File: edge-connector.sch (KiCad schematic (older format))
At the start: 3 parts, among them J5 SFF-TA-1002-4C+

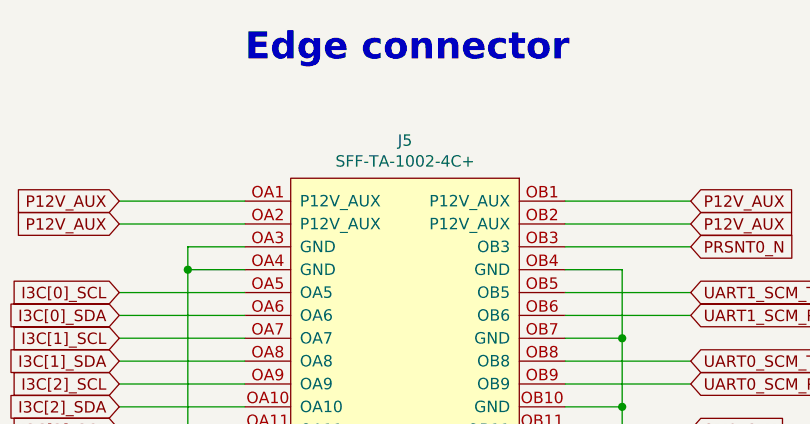
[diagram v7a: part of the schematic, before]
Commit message: Update edge connector
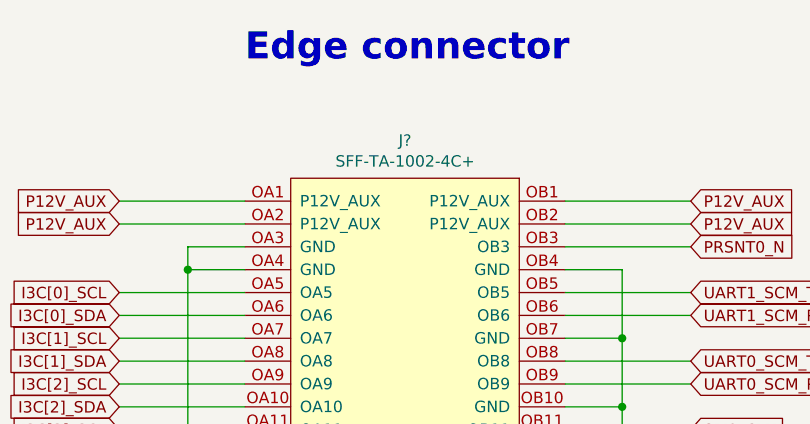
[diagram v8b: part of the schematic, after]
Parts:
- removed J5: SFF-TA-1002-4C+, artix-dc-scm-footprints:SFF-TA-1002-4C+, symbol artix-dc-scm:SFF-TA-1002-4C+
- added J?: SFF-TA-1002-4C+, artix-dc-scm-footprints:SFF-TA-1002-4C+, symbol artix-dc-scm:SFF-TA-1002-4C+
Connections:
- net 3V0_BAT: now also J?.B41
- net CHASI#: now also J?.A54
- net DBP_PRDY_N: now also J?.A50
- net DBP_PREQ_N: now also J?.A49
- net ESPI_ALERT_N: now also J?.B3
- net ESPI_CLK: now also J?.B1
- net ESPI_CS0_N: now also J?.B2
- net ESPI_CS1_N: now also J?.B9
- net ESPI_IO0: now also J?.B5
- net ESPI_IO1: now also J?.B6
- net ESPI_IO2: now also J?.B7
- net ESPI_IO3: now also J?.B8
- net ESPI_RESET_N: now also J?.B4
- net GND: now also J?.A11 (GND), J?.A14 (GND), J?.A17 (GND), J?.A20 (GND), J?.A33 (GND), J?.A42 (GND), J?.A58 (GND), J?.A61 (GND), J?.A64 (GND), J?.A67 (GND), J?.A70 (GND), J?.B10 (GND), J?.B17 (GND), J?.B26 (GND), J?.B33 (GND), J?.B38 (GND), J?.B49 (GND), J?.B52 (GND), J?.B55 (GND), J?.B58 (GND), J?.B61 (GND), J?.B64 (GND), J?.B67 (GND), J?.B70 (GND), J?.OA13 (GND), J?.OA3 (GND), J?.OA4 (GND), J?.OB10 (GND), J?.OB4 (GND), J?.OB7 (GND)
- net HPM_FW_RECOVERY: now also J?.A43
- net HPM_STBY_EN: now also J?.A45
- net HPM_STBY_RDY: now also J?.A44
- net HPM_STBY_RST_N: now also J?.A46
- net I2C[0]_SCL: now also J?.A1
- net I2C[0]_SDA: now also J?.A2
- net I2C[10]_SCL: now also J?.A31
- net I2C[10]_SDA: now also J?.A32
- net I2C[11]_SCL: now also J?.A38
- net I2C[11]_SDA: now also J?.A39
- net I2C[12]_SCL: now also J?.A40
- net I2C[12]_SDA: now also J?.A41
- net I2C[1]_SCL: now also J?.A3
- net I2C[1]_SDA: now also J?.A4
- net I2C[2]_SCL: now also J?.A5
- net I2C[2]_SDA: now also J?.A6
- net I2C[3]_SCL: now also J?.A7
- net I2C[3]_SDA: now also J?.A8
- net I2C[4]_SCL: now also J?.A9
- net I2C[4]_SDA: now also J?.A10
- net I2C[5]_SCL: now also J?.A21
- net I2C[5]_SDA: now also J?.A22
- net I2C[6]_SCL: now also J?.A23
- net I2C[6]_SDA: now also J?.A24
- net I2C[7]_SCL: now also J?.A25
- net I2C[7]_SDA: now also J?.A26
- net I2C[8]_SCL: now also J?.A27
- net I2C[8]_SDA: now also J?.A28
- net I2C[9]_SCL: now also J?.A29
- net I2C[9]_SDA: now also J?.A30
- net I3C[0]_SCL: now also J?.OA5
- net I3C[0]_SDA: now also J?.OA6
- net I3C[1]_SCL: now also J?.OA7
- net I3C[1]_SDA: now also J?.OA8
- net I3C[2]_SCL: now also J?.OA9
- net I3C[2]_SDA: now also J?.OA10
- net I3C[3]_SCL: now also J?.OA11
- net I3C[3]_SDA: now also J?.OA12
- net IRQ_N: now also J?.A56
- net JTAG_TCK: now also J?.A34
- net JTAG_TDI: now also J?.A36
- net JTAG_TDO: now also J?.A37
- net JTAG_TMS: now also J?.A35
- net NCSI_CLK: now also J?.B18
- net NCSI_CRS_DV: now also J?.B19
- net NCSI_RXD0: now also J?.B24
- net NCSI_RXD1: now also J?.B25
- net NCSI_RXER: now also J?.B23
- net NCSI_TXD0: now also J?.B21
- net NCSI_TXD1: now also J?.B22
- net NCSI_TXEN: now also J?.B20
- net P12V_AUX: now also J?.OA1 (P12V_AUX), J?.OA2 (P12V_AUX), J?.OB1 (P12V_AUX), J?.OB2 (P12V_AUX)
- net PCIE_BMC_CLK_100_N: now also J?.A13
- net PCIE_BMC_CLK_100_P: now also J?.A12
- net PCIE_BMC_RX_N: now also J?.A19
- net PCIE_BMC_RX_P: now also J?.A18
- net PCIE_BMC_TX_N: now also J?.A16
- net PCIE_BMC_TX_P: now also J?.A15
- net PCIE_HPM_CLK_N: now also J?.B57
- net PCIE_HPM_CLK_P: now also J?.B56
- net PCIE_HPM_RX[0]_N: now also J?.A60
- net PCIE_HPM_RX[0]_P: now also J?.A59
- net PCIE_HPM_RX[1]_N: now also J?.A63
- net PCIE_HPM_RX[1]_P: now also J?.A62
- net PCIE_HPM_RX[2]_N: now also J?.A66
- net PCIE_HPM_RX[2]_P: now also J?.A65
- net PCIE_HPM_RX[3]_N: now also J?.A69
- net PCIE_HPM_RX[3]_P: now also J?.A68
- net PCIE_HPM_TX[0]_N: now also J?.B60
- net PCIE_HPM_TX[0]_P: now also J?.B59
- net PCIE_HPM_TX[1]_N: now also J?.B63
- net PCIE_HPM_TX[1]_P: now also J?.B62
- net PCIE_HPM_TX[2]_N: now also J?.B66
- net PCIE_HPM_TX[2]_P: now also J?.B65
- net PCIE_HPM_TX[3]_N: now also J?.B69
- net PCIE_HPM_TX[3]_P: now also J?.B68
- net PECI_BMC: now also J?.B27
- net PRSNT0_N: now also J?.OB3
- net PRSNT1_N: now also J?.A57
- net PVCCIO_PECI: now also J?.B28
- net QSPI0_CLK: now also J?.B11
- net QSPI0_CS0_N: now also J?.B12
- net QSPI0_CS1_N: now also J?.B42
- net QSPI0_D0: now also J?.B13
- net QSPI0_D1: now also J?.B14
- net QSPI0_D2: now also J?.B15
- net QSPI0_D3: now also J?.B16
- net QSPI1_CLK: now also J?.B43
- net QSPI1_CS0_N: now also J?.B44
- net QSPI1_D0: now also J?.B45
- net QSPI1_D1: now also J?.B46
- net QSPI1_D2: now also J?.B47
- net QSPI1_D3: now also J?.B48
- net RST_PLTRST_BUF_N: now also J?.A51
- net RoT_CPU_RST_N: now also J?.A53
- net SGPIO0_CLK: now also J?.B30
- net SGPIO0_DI: now also J?.B31
- net SGPIO0_DO: now also J?.B29
- net SGPIO0_LD: now also J?.B32
- net SGPIO1_DI: now also J?.B36
- net SGPIO1_DO: now also J?.B34
- net SGPIO1_LD: now also J?.B37
- net SGPIO_INTR_N: now also J?.B40
- net SGPIO_RESET_N: now also J?.B39
- net SPARE0: now also J?.A55
- net SPARE1: now also J?.A52
- net SPI0_CLK: now also J?.OB11
- net SPI0_CS_N: now also J?.OB12
- net SPI0_MISO: now also J?.OB14
- net SPI0_MOSI: now also J?.OB13
- net SYS_PWRBTN_N: now also J?.A47
- net SYS_PWROK: now also J?.A48
- net UART0_SCM_RX: now also J?.OB9
- net UART0_SCM_TX: now also J?.OB8
- net UART1_SCM_RX: now also J?.OB6
- net UART1_SCM_TX: now also J?.OB5
- net USB1_D_N: now also J?.B54
- net USB1_D_P: now also J?.B53
- net USB2_D_N: now also J?.B51
- net USB2_D_P: now also J?.B50
- net VIRTUAL_RESEAT: now also J?.OA14
- net at R136.1: now also J?.B35
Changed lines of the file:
@@
 Comment4 ""
 $EndDescr
-$Comp
-L artix-dc-scm:SFF-TA-1002-4C+ J5
-U 1 1 625AED2C
-P 7875 1425
-F 0 "J5" H 7875 1590 50  0000 C CNN
-F 1 "SFF-TA-1002-4C+" H 7875 1499 50  0000 C CNN
-F 2 "artix-dc-scm-footprints:SFF-TA-1002-4C+" H 8275 1475 50  0001 C CNN
-F 3 "https://cdn.amphenol-icc.com/media/wysiwyg/files/documentation/sme005.pdf?__cf_chl_jschl_tk__=4604d1306574a1ee474ea914090d3e0c57e266a6-1606907014-0-AbkYBTCTl__kMBcY3BDmgKpfUy32FqitwN2Lniuy8W-uyv2Ev04Q-Q5Mr7srIz_Wnur0_9chB4CRbxKSYcEh7IvAJYsUgJ0PWIS5YdRqqHg567uaZciEX2hQP4ss5l6M4XdNrxEjJppHvyRV3ku89t-VmUSzhgCb8oJlyHpTxST4dEmKZNXfM53TM0tmGirdVbCRt1Byrx5pkz_uMvNABIOj7B2-eDGK52J3DWRD76zEyjdxY7Iz11gPiOY5i_QGIR3uOwkR5LBPNXe8zGqAf8--AKa7RqDbIriQRt90_32C4zIuHqbGa05BXS135E65ov80PbVcb4eSiutCqcJUAacUwu3eVnXVeIumfihJxuP8Rv7_n6saeG_2IuQpEiskzovLGKZM3667Y-rm-AL1NRXTamtvBxqTk0vyMvZ60FgJ" H 7875 1525 50  0001 C CNN
-	1    7875 1425
-	1    0    0    -1
-$EndComp
 Wire Wire Line
 	7175 1525 6625 1525
@@
 Text GLabel 9125 9325 2    50   Input ~ 0
 PCIE_HPM_TX[0]_P
+$Comp
+L artix-dc-scm:SFF-TA-1002-4C+ J?
+U 1 1 601205AF
+P 7875 1425
+F 0 "J?" H 7875 1590 50  0000 C CNN
+F 1 "SFF-TA-1002-4C+" H 7875 1499 50  0000 C CNN
+F 2 "artix-dc-scm-footprints:SFF-TA-1002-4C+" H 8025 1475 50  0001 C CNN
+F 3 "https://cdn.amphenol-icc.com/media/wysiwyg/files/documentation/sme005.pdf?__cf_chl_jschl_tk__=4604d1306574a1ee474ea914090d3e0c57e266a6-1606907014-0-AbkYBTCTl__kMBcY3BDmgKpfUy32FqitwN2Lniuy8W-uyv2Ev04Q-Q5Mr7srIz_Wnur0_9chB4CRbxKSYcEh7IvAJYsUgJ0PWIS5YdRqqHg567uaZciEX2hQP4ss5l6M4XdNrxEjJppHvyRV3ku89t-VmUSzhgCb8oJlyHpTxST4dEmKZNXfM53TM0tmGirdVbCRt1Byrx5pkz_uMvNABIOj7B2-eDGK52J3DWRD76zEyjdxY7Iz11gPiOY5i_QGIR3uOwkR5LBPNXe8zGqAf8--AKa7RqDbIriQRt90_32C4zIuHqbGa05BXS135E65ov80PbVcb4eSiutCqcJUAacUwu3eVnXVeIumfihJxuP8Rv7_n6saeG_2IuQpEiskzovLGKZM3667Y-rm-AL1NRXTamtvBxqTk0vyMvZ60FgJ" H 8075 1375 50  0001 C CNN
+	1    7875 1425
+	1    0    0    -1
+$EndComp
 $EndSCHEMATC
